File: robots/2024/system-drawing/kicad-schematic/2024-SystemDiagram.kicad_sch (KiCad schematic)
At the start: 181 parts

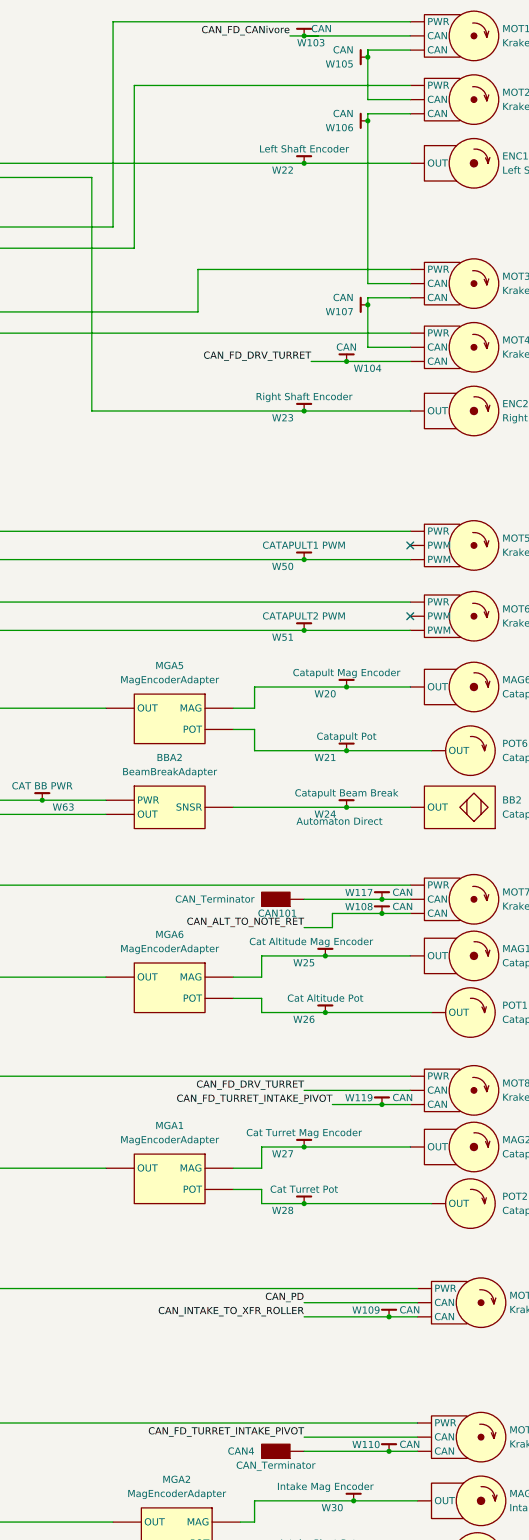
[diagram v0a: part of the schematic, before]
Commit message: Update the CAN-FD bus wiring
Signed-off-by: Scott Berman <sgberman1@gmail.com>
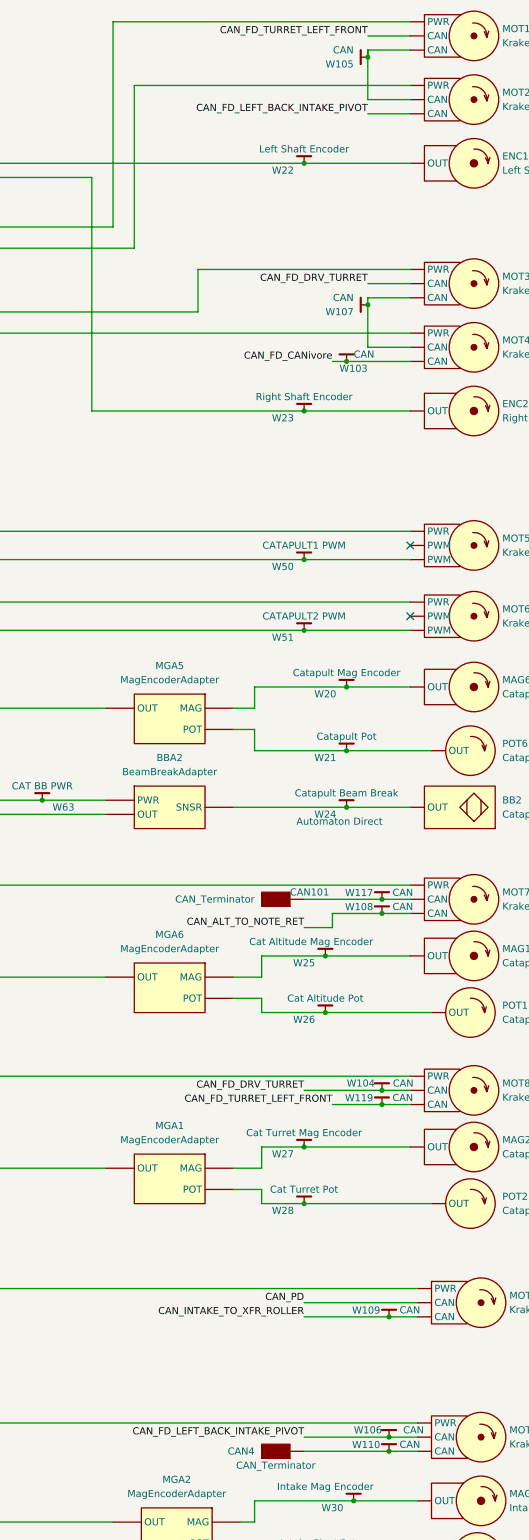
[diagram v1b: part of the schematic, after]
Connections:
- net CAN_FD_CANivore: now also MOT4. (PWR); no longer MOT1. (PWR)
- net CAN_FD_DRV_TURRET: now also MOT3. (PWR); no longer MOT4. (PWR)
- net at POE1. (RJ45S): now also RDO1. (POWER); no longer VRM1. (5V/2A)
- net at RDO1. (POWER): now also ETH1. (POWER); no longer VRM1. (5V/2A)
- net at ETH1. (POWER): now also NX1. (Power), W87.; no longer RDO1. (POWER)
- removed net CAN_FD_TURRET_INTAKE_PIVOT: MOT14. (PWR), MOT8. (PWR), W119.
- new net: VRM1. (5V/2A), W118., WG1. (4)
- new net: POE1. (RJ45S), VRM1. (5V/2A)
- new net: RDO1. (POWER), VRM1. (5V/2A)
- new net: CAN1. (USB), W67., WG1. (4)
- new net: IND1. (P), MOT11. (PWR), W114.
- new net: MOT11. (PWR), MOT13. (PWR), W113.
- new net: ETH1. (POWER), NX2. (Power), W88.
- new net: MOT10. (PWR), MOT12. (PWR), W111.
- new net: MOT12. (PWR), MOT13. (PWR), W112.
- new net: IND1. (P), MOT15. (PWR), W115.
- new net: ETH1. (POWER), VRM2. (5V/2A), W84.
- new net: ETH1. (POWER), NX3. (Power), W89.
- new net: MOT1. (PWR), MOT2. (PWR), W105.
- new net: MOT3. (PWR), MOT4. (PWR), W107.
- new net: IMU1. (RIO_PWM2), NX3. (Power), W47.
- new net CAN_FD_LEFT_BACK_INTAKE_PIVOT: MOT14. (PWR), MOT2. (PWR), W106.
- new net CAN_FD_TURRET_LEFT_FRONT: MOT1. (PWR), MOT8. (PWR), W119.
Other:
- title: 2023 FRC971 Robot -> 2024 FRC971 Robot
- moved on the sheet: W103

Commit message: Adding updated system drawing schematic and pdf
Signed-off-by: Scott Berman <sgberman1@gmail.com>
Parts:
- added WG101: VRM2/CANdleSplice, symbol SystemDiagram:Wago_3
- W24: MFG Automaton Direct -> Automation Direct
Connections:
- net CANdle PWR: now also WG101. (3); no longer PD2. (IN)
- net VRM2_PWR: no longer PD1.VRM2, VRM2. (5V/2A), W85.
- net at POE1. (RJ45S): now also RDO1. (POWER); no longer VRM1. (5V/2A)
- net at RDO1. (POWER): now also ETH1. (POWER); no longer VRM1. (5V/2A)
- net at ETH1. (POWER): now also NX1. (Power), W87.; no longer RDO1. (POWER)
- new net: VRM1. (5V/2A), W118., WG1. (4)
- new net: POE1. (RJ45S), VRM1. (5V/2A)
- new net: RDO1. (POWER), VRM1. (5V/2A)
- new net: CAN1. (USB), W67., WG1. (4)
- new net: IND1. (P), MOT11. (PWR), W114.
- new net: MOT11. (PWR), MOT13. (PWR), W113.
- new net: ETH1. (POWER), NX2. (Power), W88.
- new net: MOT10. (PWR), MOT12. (PWR), W111.
- new net: MOT12. (PWR), MOT13. (PWR), W112.
- new net: VRM2. (5V/2A), W85., WG101. (3)
- new net: IND1. (P), MOT15. (PWR), W115.
- new net: ETH1. (POWER), VRM2. (5V/2A), W84.
- new net: ETH1. (POWER), NX3. (Power), W89.
- new net: PD2. (IN), WG101. (3)
- new net: MOT1. (PWR), MOT2. (PWR), W105.
- new net: MOT3. (PWR), MOT4. (PWR), W107.
- new net: IMU1. (RIO_PWM2), NX3. (Power), W47.
- now unconnected: VRM2. (5V/2A)
- no-connect marks 69 -> 70

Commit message: Cleaned up system drawing
Signed-off-by: Scott <sgberman1@gmail.com>
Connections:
- net at POE1. (RJ45S): now also RDO1. (POWER); no longer VRM1. (5V/2A)
- net at RDO1. (POWER): now also ETH1. (POWER); no longer VRM1. (5V/2A)
- net at ETH1. (POWER): now also NX1. (Power), W87.; no longer RDO1. (POWER)
- new net: VRM1. (5V/2A), W118., WG1. (4)
- new net: POE1. (RJ45S), VRM1. (5V/2A)
- new net: RDO1. (POWER), VRM1. (5V/2A)
- new net: CAN1. (USB), W67., WG1. (4)
- new net: IND1. (P), MOT11. (PWR), W114.
- new net: MOT11. (PWR), MOT13. (PWR), W113.
- new net: ETH1. (POWER), NX2. (Power), W88.
- new net: MOT10. (PWR), MOT12. (PWR), W111.
- new net: MOT12. (PWR), MOT13. (PWR), W112.
- new net: VRM2. (5V/2A), W85., WG101. (3)
- new net: IND1. (P), MOT15. (PWR), W115.
- new net: ETH1. (POWER), VRM2. (5V/2A), W84.
- new net: ETH1. (POWER), NX3. (Power), W89.
- new net: PD2. (IN), WG101. (3)
- new net: MOT1. (PWR), MOT2. (PWR), W105.
- new net: MOT3. (PWR), MOT4. (PWR), W107.
- new net: IMU1. (RIO_PWM2), NX3. (Power), W47.
- now unconnected: VRM2. (5V/2A), VRM2. (5V/2A)
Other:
- moved on the sheet: CAM1, CAM2, CAM3, CAM4

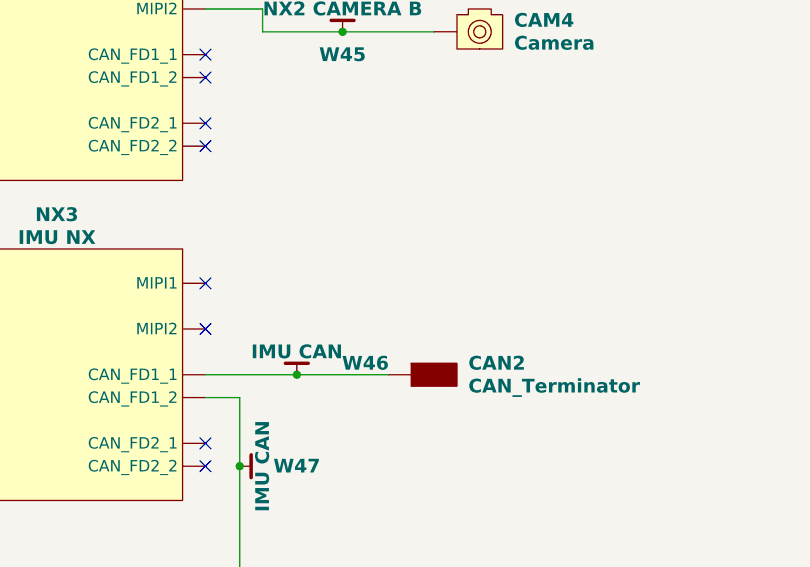
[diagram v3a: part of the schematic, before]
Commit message: Added driver camera to system drawing
Signed-off-by: Scott Berman <sgberman1@gmail.com>
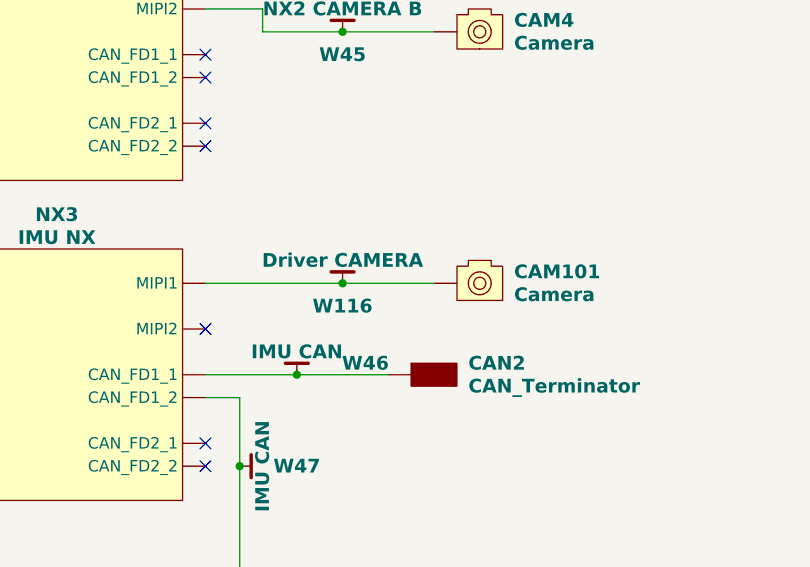
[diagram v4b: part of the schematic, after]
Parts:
- added CAM101: Camera, symbol SystemDiagram:Camera
- added W116: Driver CAMERA, symbol SystemDiagram:WireTag
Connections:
- net at POE1. (RJ45S): now also RDO1. (POWER); no longer VRM1. (5V/2A)
- net at RDO1. (POWER): now also ETH1. (POWER); no longer VRM1. (5V/2A)
- net at ETH1. (POWER): now also NX1. (Power), W87.; no longer RDO1. (POWER)
- new net: VRM1. (5V/2A), W118., WG1. (4)
- new net: POE1. (RJ45S), VRM1. (5V/2A)
- new net: RDO1. (POWER), VRM1. (5V/2A)
- new net: CAN1. (USB), W67., WG1. (4)
- new net: IND1. (P), MOT11. (PWR), W114.
- new net: MOT11. (PWR), MOT13. (PWR), W113.
- new net: ETH1. (POWER), NX2. (Power), W88.
- new net: MOT10. (PWR), MOT12. (PWR), W111.
- new net: MOT12. (PWR), MOT13. (PWR), W112.
- new net: VRM2. (5V/2A), W85., WG101. (3)
- new net: IND1. (P), MOT15. (PWR), W115.
- new net: ETH1. (POWER), VRM2. (5V/2A), W84.
- new net: ETH1. (POWER), NX3. (Power), W89.
- new net: PD2. (IN), WG101. (3)
- new net: MOT1. (PWR), MOT2. (PWR), W105.
- new net: CAM101., NX3. (Power), W116.
- new net: MOT3. (PWR), MOT4. (PWR), W107.
- new net: IMU1. (RIO_PWM2), NX3. (Power), W47.
- now unconnected: VRM2. (5V/2A), VRM2. (5V/2A)
- no-connect marks 70 -> 69
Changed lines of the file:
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@@
   (junction (at 601.98 356.87) (diameter 0) (color 0 0 0 0)
   )
+  (junction (at 240.03 452.12) (diameter 0) (color 0 0 0 0)
+  )
   (junction (at 601.98 267.97) (diameter 0) (color 0 0 0 0)
   )
@@
   (junction (at 487.68 262.89) (diameter 0) (color 255 0 0 1)
   )
-  (no_connect (at 224.79 452.12))
   (no_connect (at 220.98 269.24))
   (no_connect (at 220.98 219.71))
@@
     (stroke (width 0) (type default))
   )
+  (wire (pts (xy 240.03 452.12) (xy 250.19 452.12))
+    (stroke (width 0.254) (type default) (color 0 194 194 1))
+  )
   (wire (pts (xy 610.87 374.65) (xy 595.63 374.65))
     (stroke (width 0) (type default))
@@
   (wire (pts (xy 610.87 311.15) (xy 595.63 311.15))
     (stroke (width 0) (type default))
+  )
+  (wire (pts (xy 224.79 452.12) (xy 240.03 452.12))
+    (stroke (width 0.254) (type default) (color 0 194 194 1))
   )
   (wire (pts (xy 605.79 154.94) (xy 594.36 154.94))
@@
     )
   )
+  (symbol (lib_id "SystemDiagram:Camera") (at 252.73 452.12 0) (unit 1)
+    (in_bom yes) (on_board yes) (dnp no)
+    (property "Reference" "CAM101" (at 259.08 450.85 0)
+      (effects (font (face "FreeSans") (size 1.524 1.524) bold) (justify left))
+    )
+    (property "Value" "Camera" (at 259.08 453.39 0)
+      (effects (font (face "FreeSans") (size 1.524 1.524) bold) (justify left))
+    )
+    (property "Footprint" "" (at 252.73 452.12 0)
+      (effects (font (size 1.27 1.27)) hide)
+    )
+    (property "Datasheet" "" (at 252.73 452.12 0)
+      (effects (font (size 1.27 1.27)) hide)
+    )
+    (pin "")
+    (instances
+      (project "2024-SystemDiagram"
+        (path "/12a52703-e3f4-4774-b510-3055ab1abf35"
+          (reference "CAM101") (unit 1)
+        )
+      )
+    )
+  )
   (symbol (lib_id "SystemDiagram:WireTag") (at 594.36 176.53 0) (unit 1)
     (in_bom yes) (on_board yes) (dnp no)
@@
         )
       )
+    )
+  )
+  (symbol (lib_id "SystemDiagram:WireTag") (at 240.03 452.12 0) (unit 1)
+    (in_bom yes) (on_board yes) (dnp no)
+    (property "Reference" "W116" (at 240.03 454.66 0)
+      (effects (font (face "FreeSans") (size 1.524 1.524) bold))
+    )
+    (property "Value" "Driver CAMERA" (at 240.03 449.58 0)
+      (effects (font (face "FreeSans") (size 1.524 1.524) bold))
+    )
+    (property "Footprint" "" (at 240.03 452.12 0)
+      (effects (font (size 1.27 1.27)) hide)
+    )
+    (property "Datasheet" "" (at 240.03 452.12 0)
+      (effects (font (size 1.27 1.27)) hide)
+    )
+    (pin "")
+    (instances
+      (project "2024-SystemDiagram"
+        (path "/12a52703-e3f4-4774-b510-3055ab1abf35"
+          (reference "W116") (unit 1)
+        )
+      )
